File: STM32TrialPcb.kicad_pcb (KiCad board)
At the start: 2 copper layers, 50.5 x 30 mm, 31 parts, among them J1 USB_B_Micro, J2 Conn_01x15, J3 Conn_01x15, SW1 SW_Push, SW2 SW_Push, U1 TLV75533PDRV, U2 STM32F103C8T6, Y1 8M

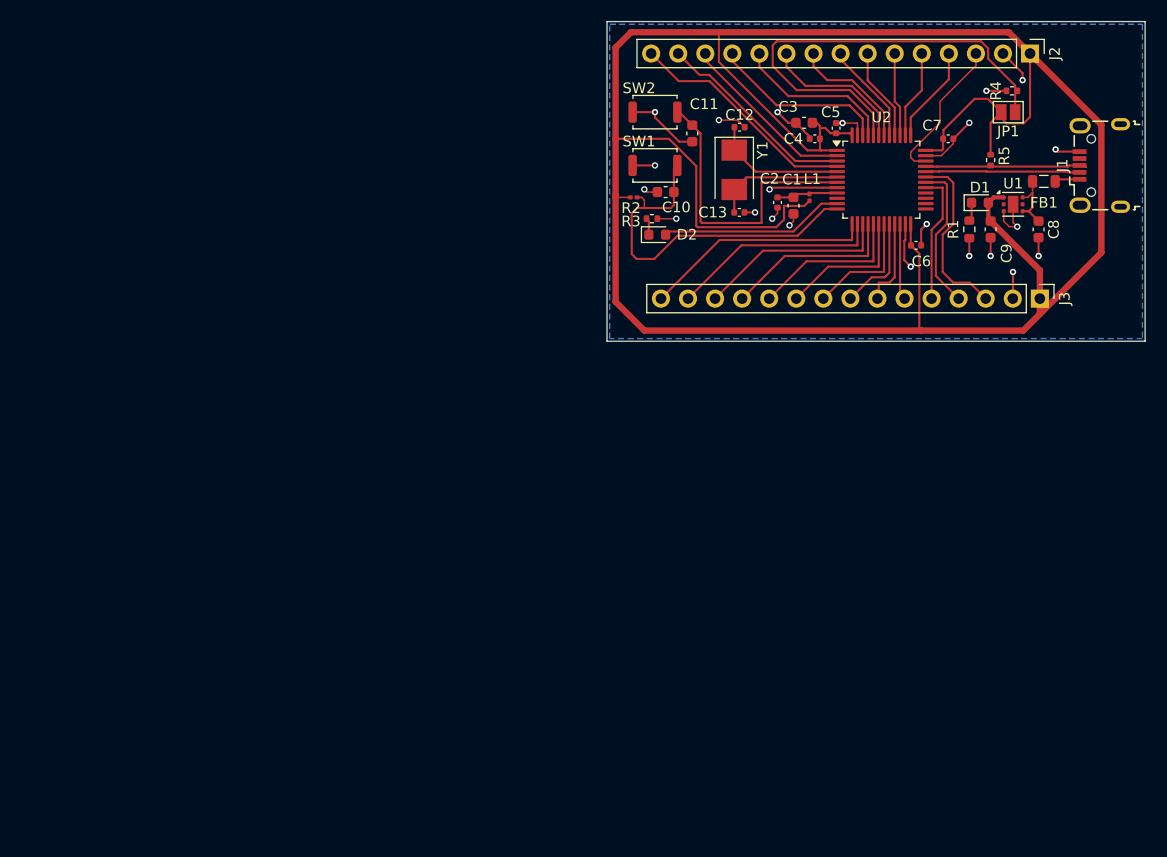
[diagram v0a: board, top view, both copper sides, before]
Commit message: Improve layout, dimensions, symmetry.
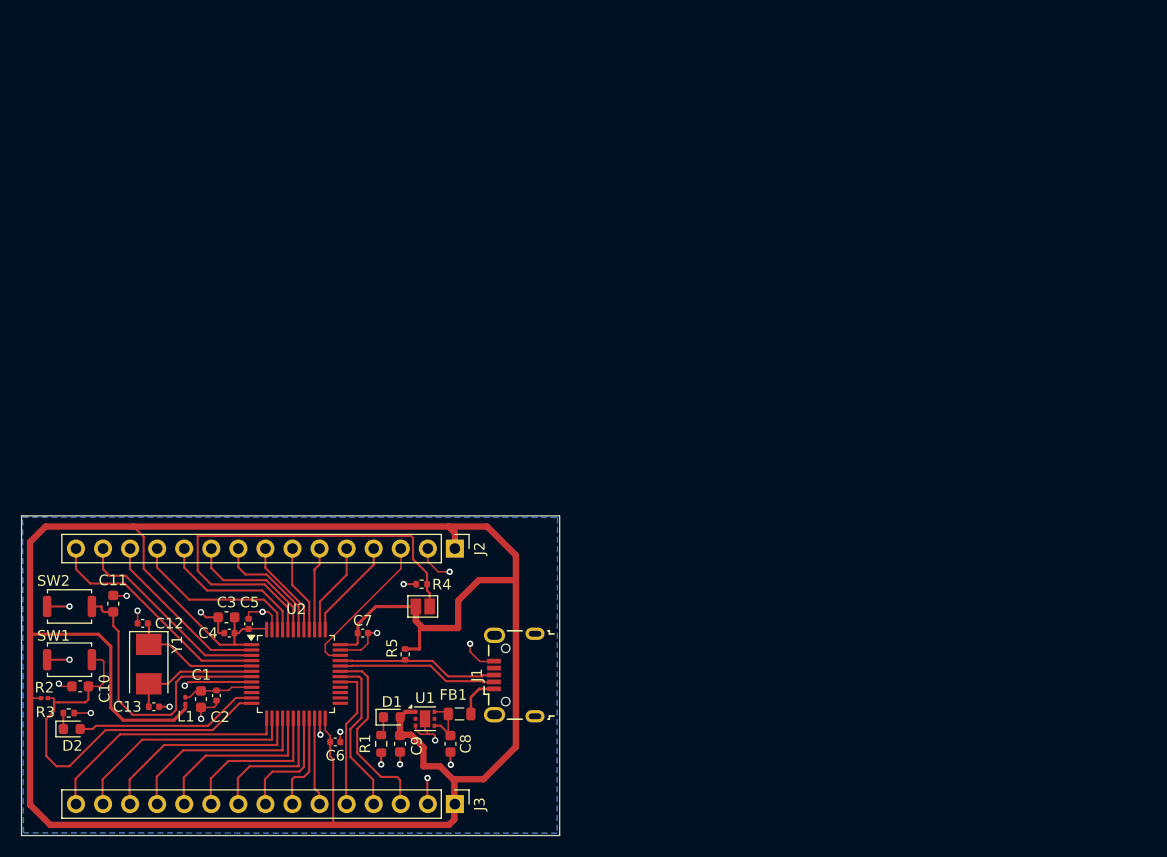
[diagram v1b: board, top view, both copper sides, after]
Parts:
- moved L1 75.3 mm to (140.9, 97.2)
- moved FB1 74.2 mm to (166.7, 98.5)
- moved C9 73.5 mm to (161.1, 101.3)
- moved U1 73.3 mm to (163.4, 98.9)
- moved C8 73.3 mm to (165.8, 101.3)
- moved D1 73.3 mm to (160.3, 98.8)
- moved R1 73.3 mm to (159.3, 101.3)
- moved J1 72.8 mm to (171.8, 94.8)
- moved C12 72.8 mm to (136.9, 90.0), turned to 180 degrees
- moved R2 72.6 mm to (127.7, 97.0)
- moved J3 72.6 mm to (166.2, 106.9)
- moved C1 72.4 mm to (142.4, 97.1)
- moved R4 72.2 mm to (163.1, 86.3)
- moved C5 72.1 mm to (146.9, 90.0)
- moved C7 71.9 mm to (157.6, 90.9)
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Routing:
- net GND: track 64.5 -> 54.2 mm
- net +3V3: track 237.0 -> 244.2 mm
- net Net-(U2-PA2): track 34.9 -> 38.1 mm
- net PA6: track 16.5 -> 18.4 mm
- net PA7: track 14.7 -> 16.6 mm
- net PB1: track 11.2 -> 13.1 mm
- net PB0: track 13.0 -> 14.8 mm
- net PA3: track 21.7 -> 23.6 mm
- net PB2: track 9.23 -> 11.1 mm
- net PA4: track 20.0 -> 21.8 mm
- net PA5: track 18.2 -> 20.0 mm
- net VCC: track 2.36 -> 4.06 mm
- net SWDIO: track 14.0 -> 15.3 mm
- net PA8: track 12.4 -> 13.5 mm
- net PB11: track 7.17 -> 8.24 mm
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
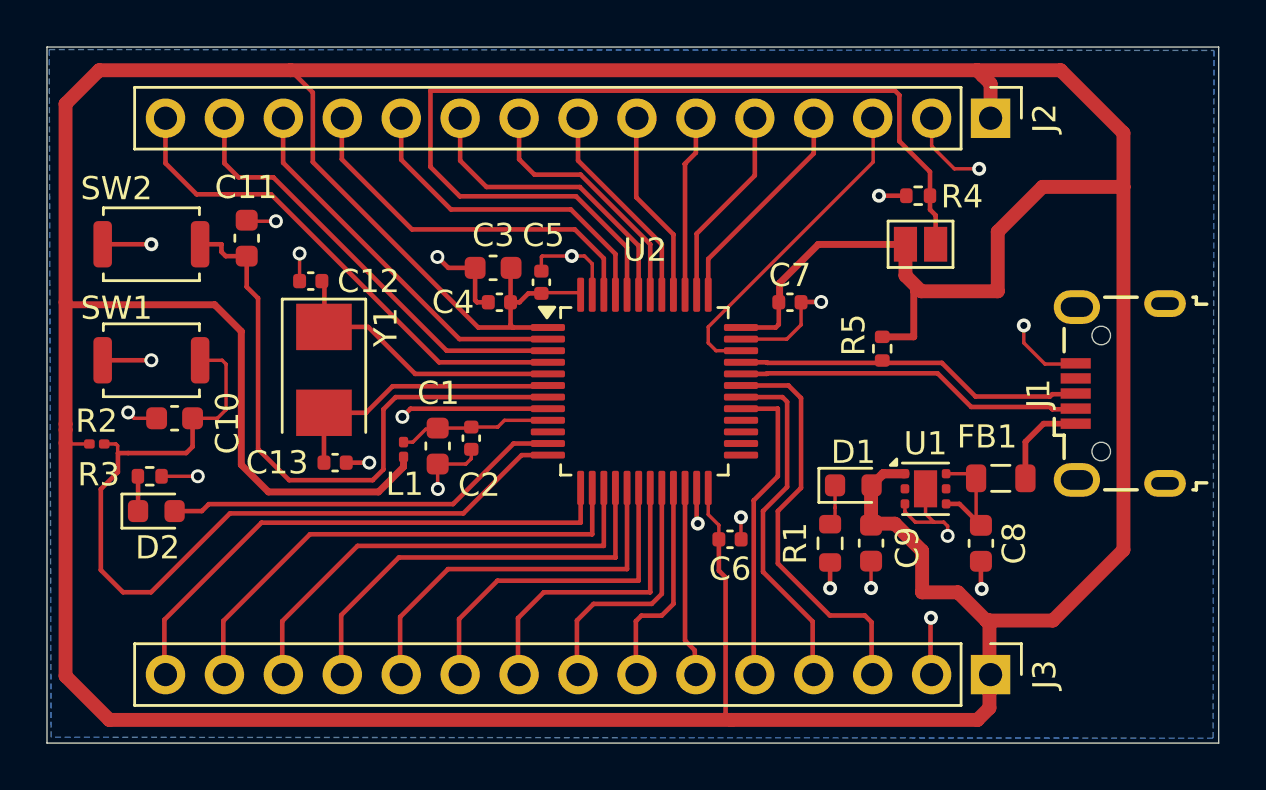
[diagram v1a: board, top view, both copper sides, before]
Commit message: fix dimensions 50x30mm etc...
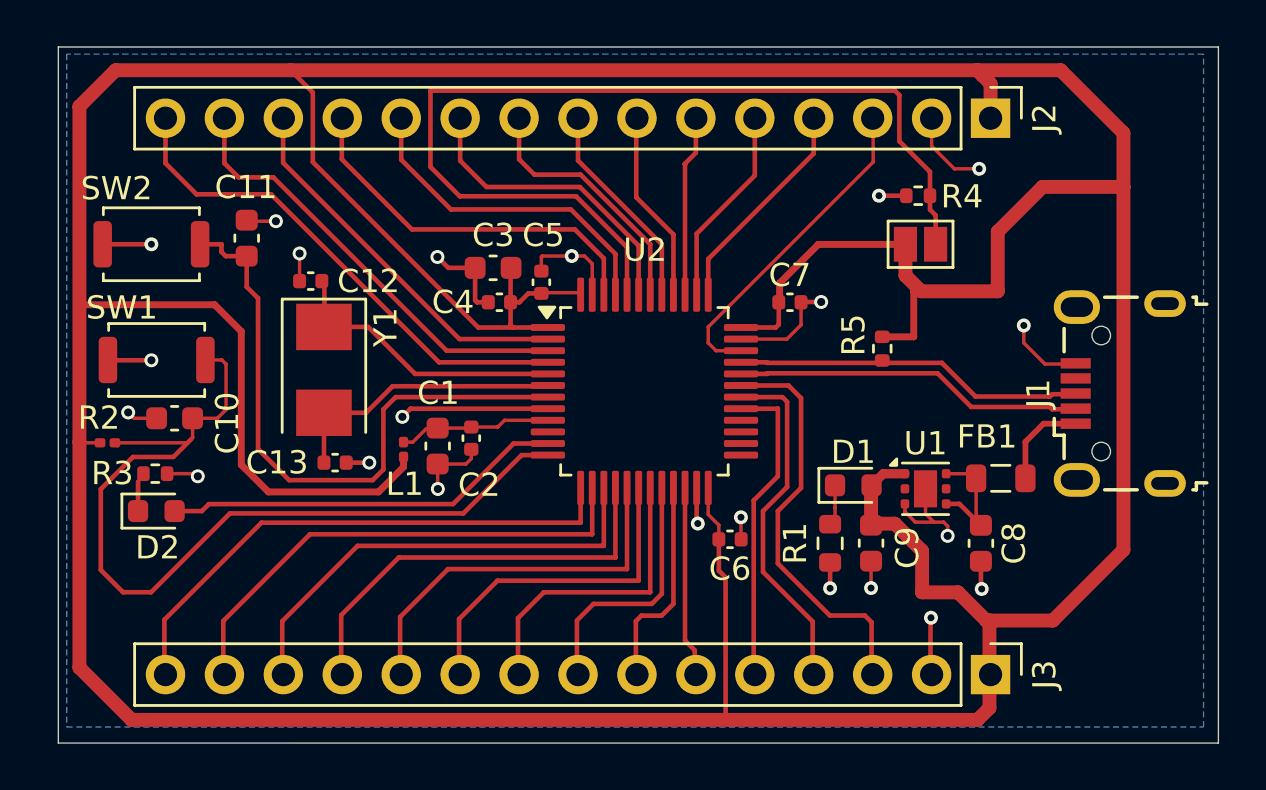
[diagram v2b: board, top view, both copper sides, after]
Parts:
- moved R2 0.46 mm to (128.2, 97.0)
- moved R3 0.27 mm to (130.2, 98.3)
- moved SW1 0.23 mm to (130.3, 93.4)
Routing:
- net +3V3: track 244.2 -> 241.6 mm
- net Net-(U2-PA2): track 38.1 -> 39.8 mm
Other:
- board size 50.5 x 30 mm -> 50 x 30 mm

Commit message: add assembly and move gerbers, update pcb
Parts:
- L1: footprint Inductor_SMD:L_0201_0603Metric -> Inductor_SMD:L_0603_1608Metric
- R2: footprint Resistor_SMD:R_0201_0603Metric -> Resistor_SMD:R_0402_1005Metric
- moved R3 2.36 mm to (129.1, 100.4)
- moved D2 2.05 mm to (129.7, 101.9)
- moved R2 1.33 mm to (129.1, 97.9)
- moved C1 1.02 mm to (143.1, 97.8)
- moved C2 0.84 mm to (144.7, 96.5)
- moved L1 0.70 mm to (141.3, 97.8)
- moved SW2 0.23 mm to (130.3, 88.4)
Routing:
- net GND: track 54.1 -> 51.9 mm
- net Net-(D2-A): track 17.3 -> 19.5 mm
- net +3V3: track 241.6 -> 242.8 mm
- net +3.3VA: track 6.61 -> 7.47 mm
